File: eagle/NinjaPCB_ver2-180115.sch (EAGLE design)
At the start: 54 parts, among them IC3 ANALOGSW_AD_SOT23-6, IC6 NAU7802, J2 ATX24, J3 HEATER, J4 HEATER_TEMP, Q1 S9013, Q2 IRF520NPBF, Q3 IRF520NPBF, Q4 S9013, Q5 IRF520NPBF, Q6 S9013, Q7 S9013, Q8 S9013, U1 CJT1117-3.3-SOT223

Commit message: to be ordered
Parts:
- removed R10: 3K, Seeed-Resistor:SMD-RES-3K-1%-1/10W(0603)
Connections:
- removed net N$1: J4.2, R10.2
- net HEATER_TEMP: now also J4.2; no longer R10.1
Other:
- note added: "Diff from ver2-170831: 1. Pullup IO0 2. Pulldown HEATER 3. Killed ADC MCP 4. INT_ADC is moved to HEATER_TEMP 5. RX/TX replaced 6. Use ESP-WROOM-02-BREAK 7. Use Relay instead of Motor Driver"
- note removed: "Diff from ver2-170831: 1. Pullup IO0 2. Pulldown HEATER 3. Killed ADC MCP 4. INT_ADC is moved to HEATER_TEMP 5. RX/TX replaced 6. USE ESP-WROOM-02-BREAK"
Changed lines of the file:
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@@
 <part name="GND15" library="supply1" deviceset="GND" device=""/>
 <part name="C3" library="Seeed-Capacitor" deviceset="CERAMIC-100NF-50V-10%-X7R(0603)" device="" value="100nf"/>
-<part name="R10" library="Seeed-Resistor" deviceset="SMD-RES-3K-1%-1/10W(0603)" device="" value="3K"/>
 <part name="R14" library="Seeed-Resistor" deviceset="SMD-RES-2K-1%-1/10W(0603)" device="" value="2K"/>
 <part name="RL" library="PCR-RCL" deviceset="R0603" device="" value="30K HP"/>
@@
 4. INT_ADC is moved to HEATER_TEMP
 5. RX/TX replaced
-6. USE ESP-WROOM-02-BREAK</text>
+6. Use ESP-WROOM-02-BREAK
+7. Use Relay instead of Motor Driver</text>
 </plain>
 <instances>
@@
 <instance part="GND15" gate="1" x="160.02" y="135.89"/>
 <instance part="C3" gate="G$1" x="160.02" y="154.94" rot="R90"/>
-<instance part="R10" gate="G$1" x="241.3" y="154.94"/>
 <instance part="R14" gate="G$1" x="241.3" y="148.59"/>
 <instance part="RL" gate="G$1" x="209.55" y="219.71" rot="R90"/>
@@
 <pinref part="IC6" gate="G$1" pin="VIN2P"/>
 <label x="213.36" y="154.94" size="1.778" layer="95"/>
-<wire x1="237.49" y1="154.94" x2="234.95" y2="154.94" width="0.1524" layer="91"/>
 <pinref part="R14" gate="G$1" pin="1"/>
 <wire x1="237.49" y1="148.59" x2="234.95" y2="148.59" width="0.1524" layer="91"/>
 <wire x1="234.95" y1="148.59" x2="234.95" y2="154.94" width="0.1524" layer="91"/>
-<pinref part="R10" gate="G$1" pin="1"/>
 <wire x1="209.55" y1="154.94" x2="234.95" y2="154.94" width="0.1524" layer="91"/>
 <junction x="234.95" y="154.94"/>
+<pinref part="J4" gate="G$1" pin="2"/>
+<wire x1="234.95" y1="154.94" x2="247.65" y2="154.94" width="0.1524" layer="91"/>
 </segment>
 </net>
@@
 </segment>
 </net>
-<net name="N$1" class="0">
-<segment>
-<pinref part="J4" gate="G$1" pin="2"/>
-<pinref part="R10" gate="G$1" pin="2"/>
-<wire x1="247.65" y1="154.94" x2="245.11" y2="154.94" width="0.1524" layer="91"/>
-</segment>
-</net>

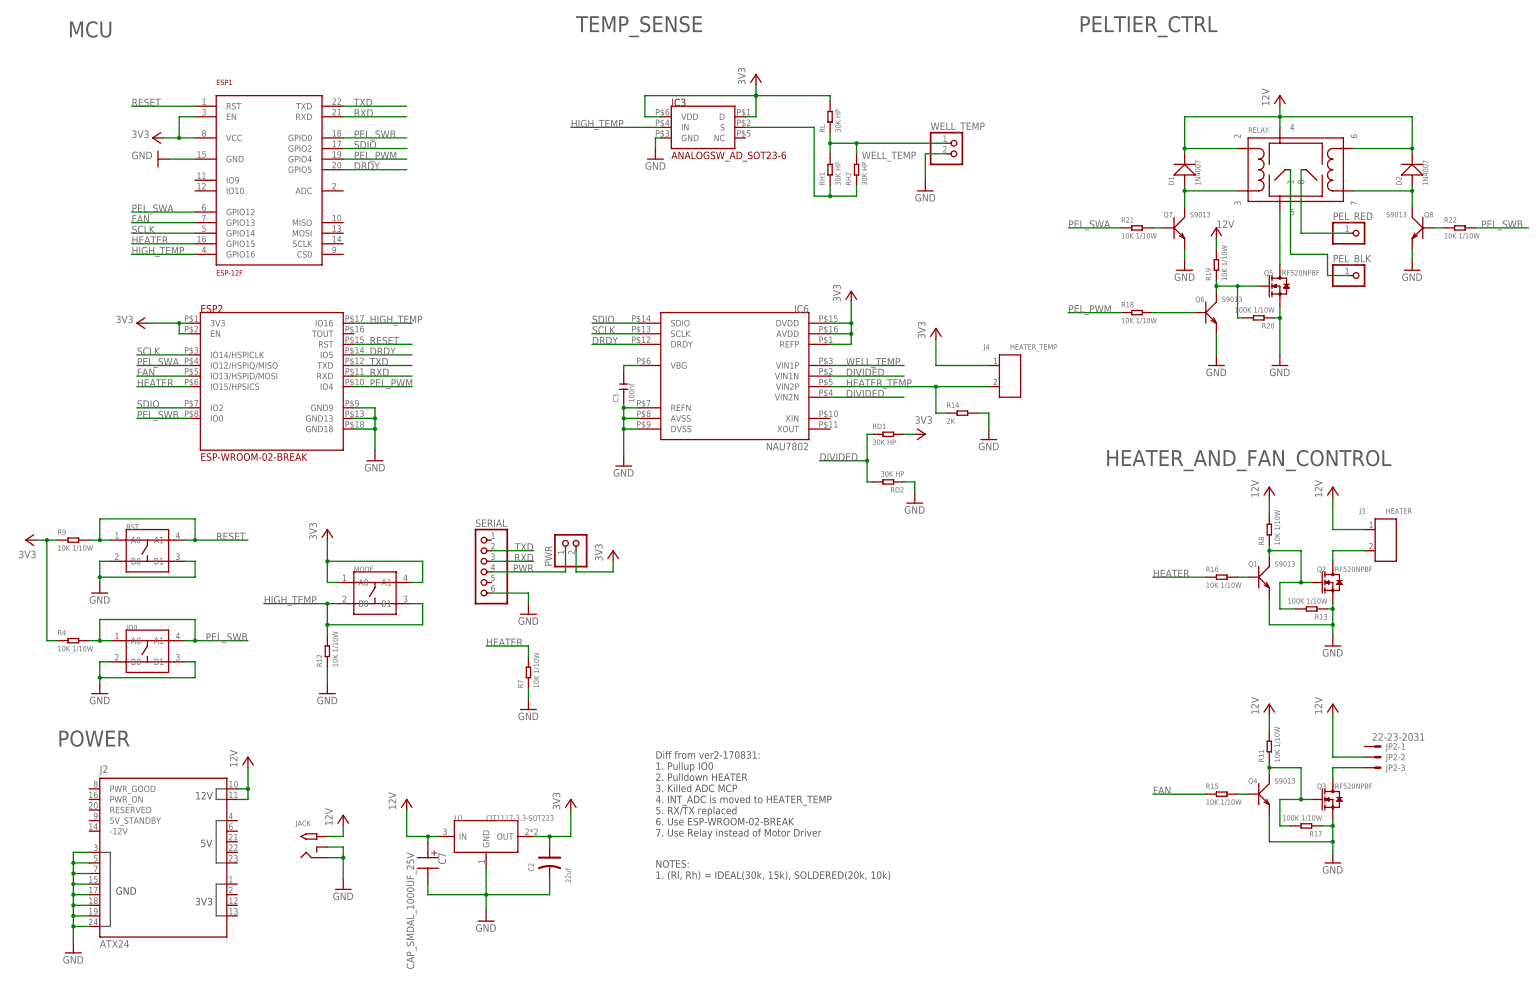
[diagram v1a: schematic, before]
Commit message: npn to pnp. added pullups and pulldowns
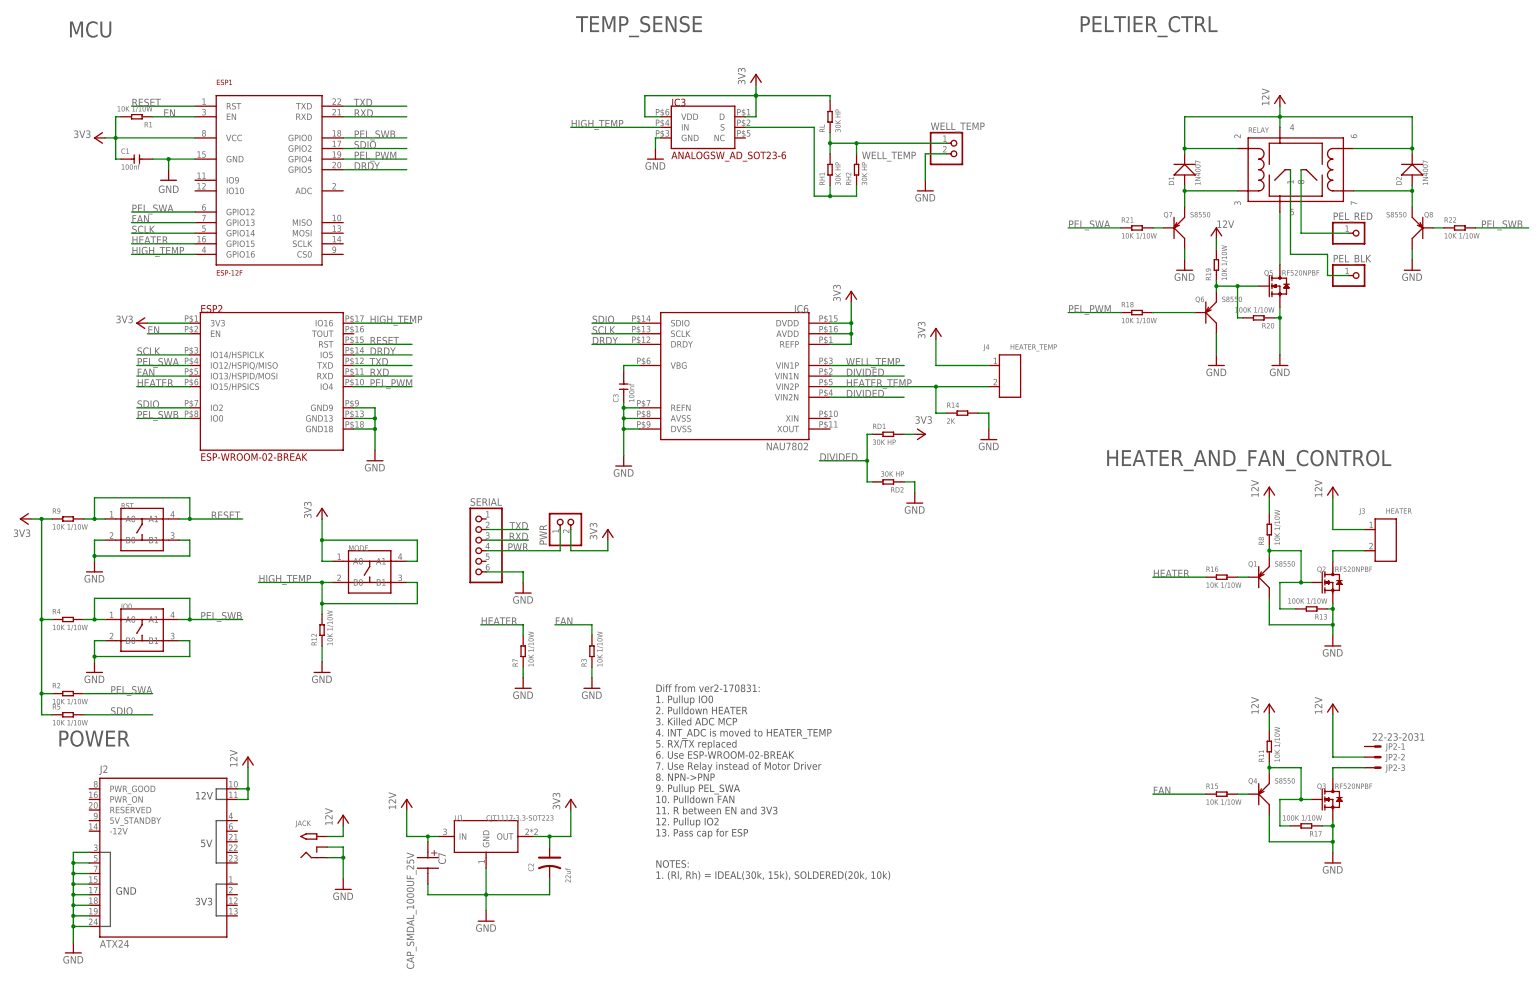
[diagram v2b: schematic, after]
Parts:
- added C1: 100nf, Seeed-Capacitor:CERAMIC-100NF-50V-10%-X7R(0603)
- added R1, R2, R3, R5: 10K 1/10W, Seeed-Resistor:SMD-RES-10K-5%-1/10W(0603)
- Q1, Q4, Q6, Q7, Q8: value S9013 -> S8550; device Seeed-Transistor:SMD-TRANSISTORS-NPN-25V-500MA-S9013(SOT-23) -> Seeed-Transistor:SMD-TRANSISTORS-PNP-25V-500MA-S8550(SOT-23)
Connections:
- new net EN: ESP1.EN, ESP2.EN, R1.1
- net 3V3: now also C1.1, R1.2, R2.1, R5.1; no longer ESP1.EN, ESP2.EN
- net FAN: now also R3.2
- net GND: now also C1.2, Q1.C, Q4.C, Q6.C, Q7.C, Q8.C, R3.1; no longer Q1.E, Q4.E, Q6.E, Q7.E, Q8.E
- net N$25: now also Q4.E; no longer Q4.C
- net N$29: now also Q1.E; no longer Q1.C
- net N$33: now also Q7.E; no longer Q7.C
- net N$36: now also Q8.E; no longer Q8.C
- net N$5: now also Q6.E; no longer Q6.C
- net PEL_SWA: now also R2.2
- net SDIO: now also R5.2
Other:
- note added: "Diff from ver2-170831: 1. Pullup IO0 2. Pulldown HEATER 3. Killed ADC MCP 4. INT_ADC is moved to HEATER_TEMP 5. RX/TX replaced 6. Use ESP-WROOM-02-BREAK 7. Use Relay instead of Motor Driver 8. NPN->PNP 9. Pullup PEL_SWA 10. Pulldown FAN 11. R between EN and 3V3 12. Pullup IO2 13. Pass cap for ESP"
- note removed: "Diff from ver2-170831: 1. Pullup IO0 2. Pulldown HEATER 3. Killed ADC MCP 4. INT_ADC is moved to HEATER_TEMP 5. RX/TX replaced 6. Use ESP-WROOM-02-BREAK 7. Use Relay instead of Motor Driver"
- moved on the sheet: IO0, MODE, PWR, R12, R4, R7, R9, RST, SERIAL
